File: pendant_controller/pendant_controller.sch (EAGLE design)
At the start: 58 parts, among them IC1 ATMEGA32U4-MU, J1 BATT__CONN, U3 MIC5205-3.3V, U4 MIC5205-3.3V, U5 LTC4054LES5-4.2TRPBF, U6 MPU-6050, U7 SPX3819-3.3, U8 HC-06-SIMPLIFIED, Y1 8MHz

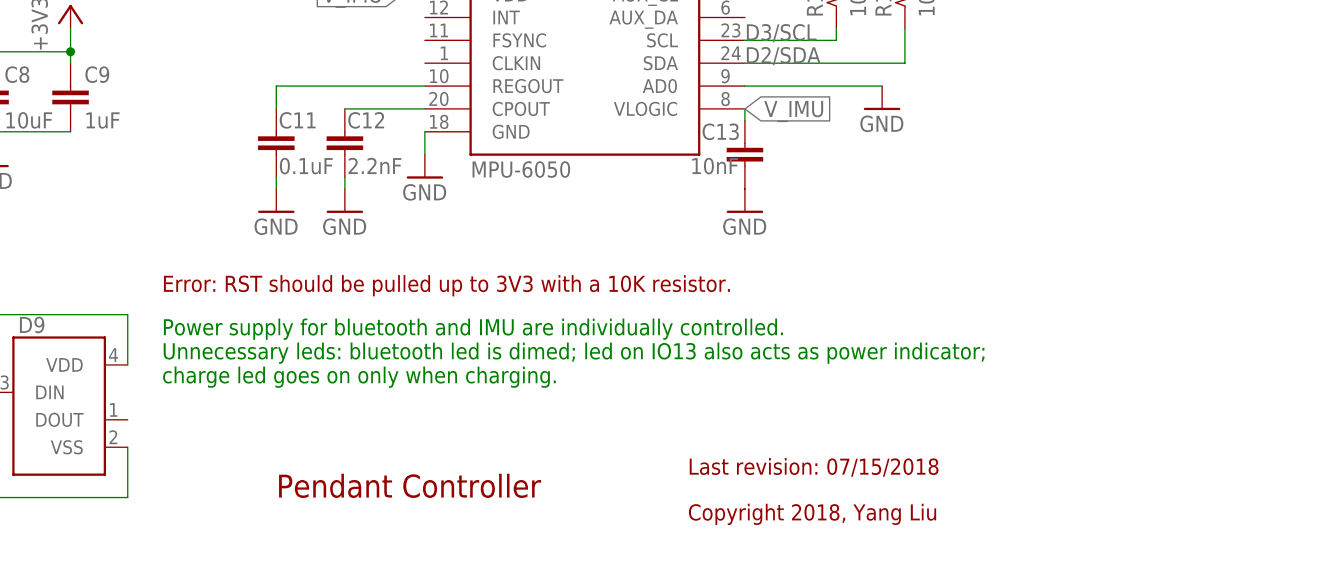
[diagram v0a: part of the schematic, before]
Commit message: fix regulator not enabled problem
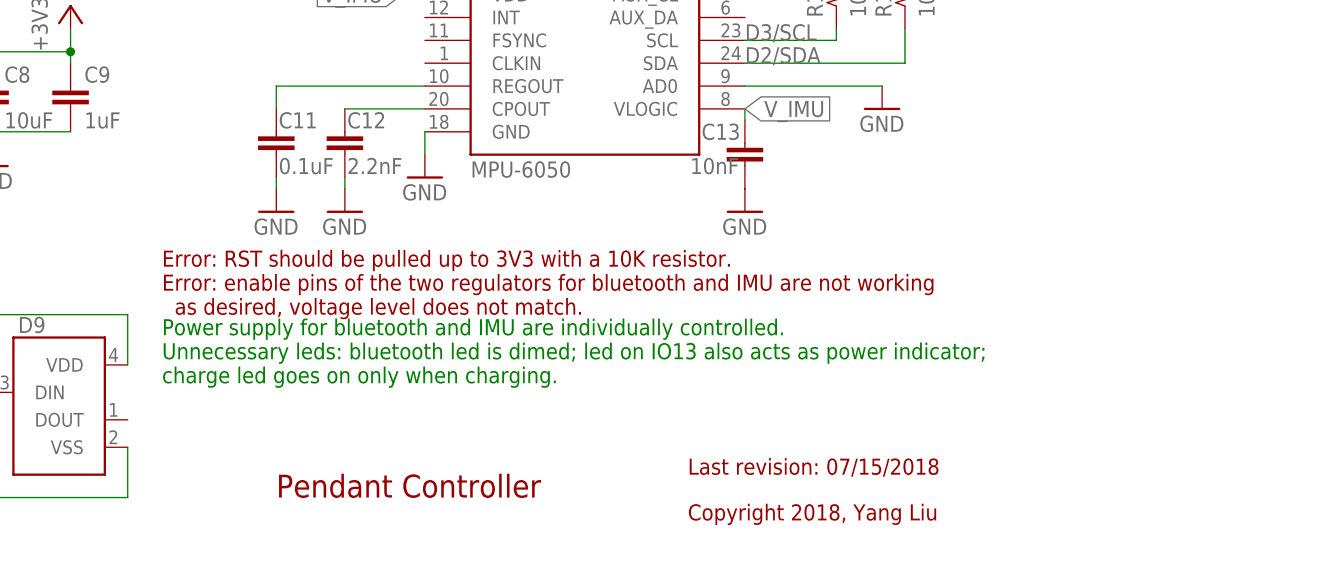
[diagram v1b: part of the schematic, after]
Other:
- note added: "Error: RST should be pulled up to 3V3 with a 10K resistor. Error: enable pins of the two regulators for bluetooth and IMU are not working as desired, voltage level does not match."
- note removed: "Error: RST should be pulled up to 3V3 with a 10K resistor."
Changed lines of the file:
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@@
 Unnecessary leds: bluetooth led is dimed; led on IO13 also acts as power indicator;
 charge led goes on only when charging.</text>
-<text x="162.56" y="35.56" size="1.778" layer="94">Error: RST should be pulled up to 3V3 with a 10K resistor.</text>
+<text x="162.56" y="33.02" size="1.778" layer="94">Error: RST should be pulled up to 3V3 with a 10K resistor.
+Error: enable pins of the two regulators for bluetooth and IMU are not working
+  as desired, voltage level does not match.</text>
 </plain>
 <instances>
